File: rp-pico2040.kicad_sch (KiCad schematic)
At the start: 0 parts

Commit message: update components, pending route signals of connectors
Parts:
- added A1: RaspberryPi_Pico, Module:RaspberryPi_Pico_Common_Unspecified, symbol MCU_Module:RaspberryPi_Pico
- added D6: GREEN, LED_SMD:LED_1206_3216Metric, symbol Device:LED
- added D7, D8: RED, LED_SMD:LED_1206_3216Metric, symbol Device:LED
- added D9: SM4005PL-TP, symbol Device:D_Schottky
- added J3: Conn_01x07, symbol Connector_Generic:Conn_01x07
- added J4, J5: Conn_01x02, symbol Connector_Generic:Conn_01x02
- added J6: Conn_01x04, symbol Connector_Generic:Conn_01x04
- added R10, R11, R12: 1k, Resistor_SMD:R_1206_3216Metric, symbol Device:R
- added SW2, SW3: SW_Push, symbol Switch:SW_Push
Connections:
- new net: D8.2 (A), R12.1
- new net: A1.15 (GPIO11), SW2.2
- new net: A1.32 (GPIO27_ADC1), R12.2
- new net: D7.2 (A), R11.1
- new net: A1.1 (GPIO0), J3.1 (Pin_1)
- new net: A1.2 (GPIO1), J3.2 (Pin_2)
- new net: A1.4 (GPIO2), J3.3 (Pin_3)
- new net: A1.5 (GPIO3), J3.4 (Pin_4)
- new net: A1.6 (GPIO4), J3.5 (Pin_5)
- new net: A1.7 (GPIO5), J3.6 (Pin_6)
- new net: A1.34 (GPIO28_ADC2), SW3.1
- new net: A1.39 (VSYS), D9.1 (K)
- new net: D9.2 (A), J4.1 (Pin_1)
- new net: A1.10 (GPIO7), R11.2
- new net: A1.9 (GPIO6), R10.2
- new net: D6.2 (A), R10.1
- new net CHARGED: A1.24 (GPIO18), A1.31 (GPIO26_ADC0)
- new net GND: A1.13 (GND), A1.18 (GND), A1.23 (GND), A1.28 (GND), A1.3 (GND), A1.33 (AGND), A1.38 (GND), A1.8 (GND), D6.1 (K), D7.1 (K), D8.1 (K), J3.7 (Pin_7), J4.2 (Pin_2), SW2.1
- new net HVPULSE: A1.19 (GPIO14)
- new net HVPWM: A1.26 (GPIO20)
- new net VCC: A1.36 (3V3), SW3.2
- no-connect marks 0 -> 15

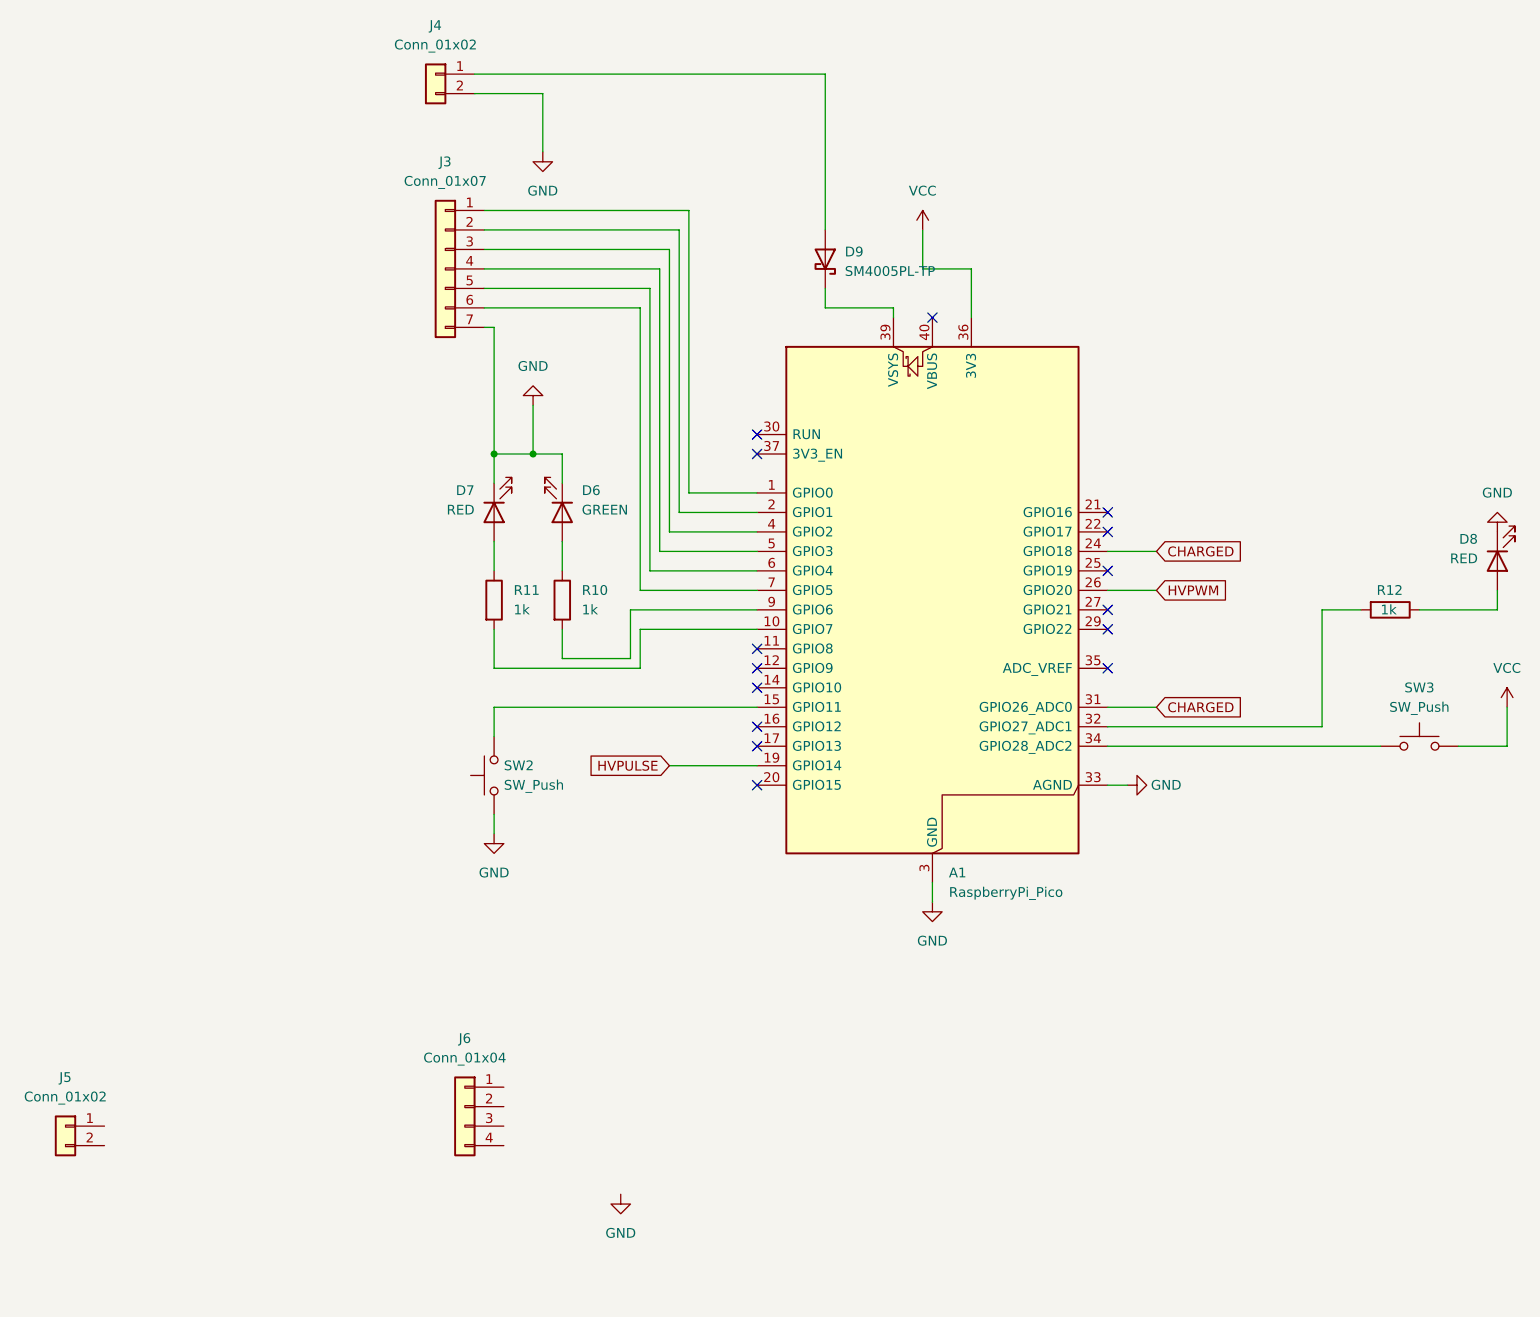
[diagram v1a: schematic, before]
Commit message: update components and footprints
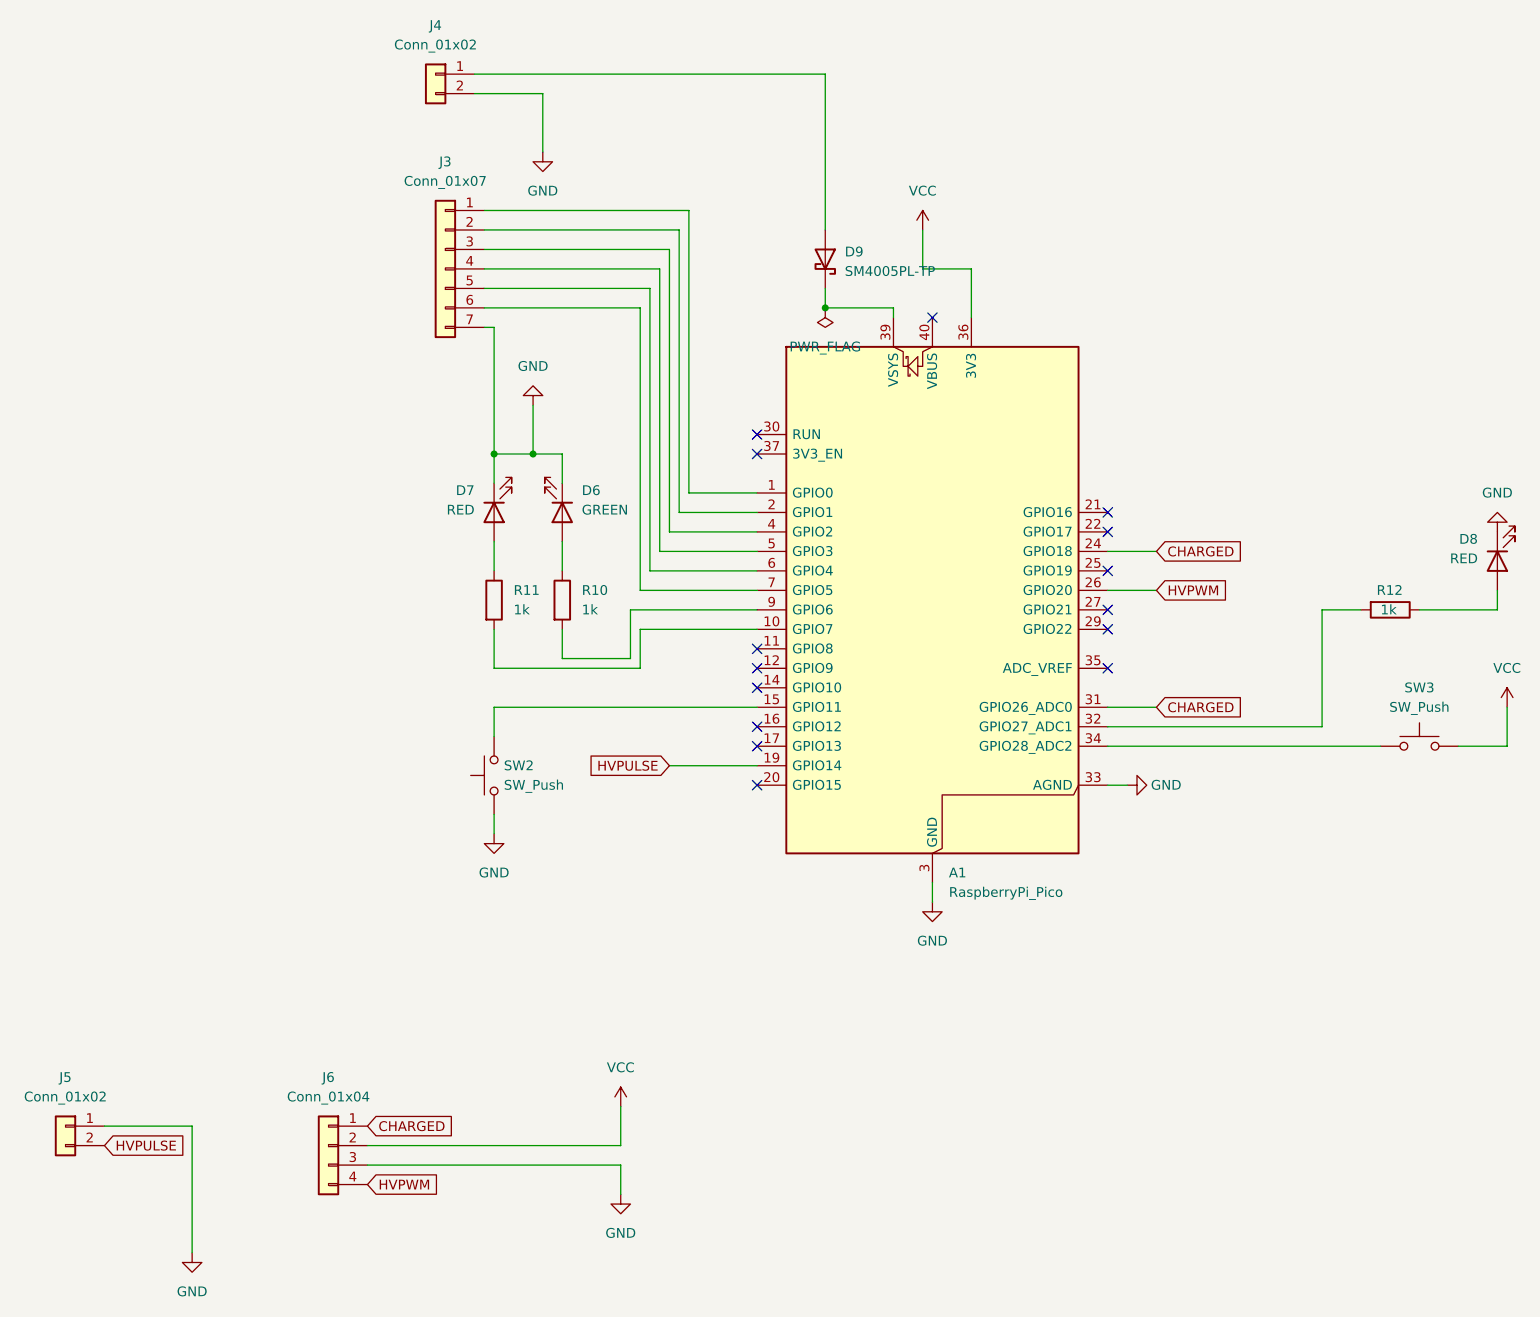
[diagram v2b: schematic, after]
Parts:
- D6: PART_NUMBER_LCSC (none) -> C3646937
- D7: PART_NUMBER_LCSC (none) -> C434444
- D8: PART_NUMBER_LCSC (none) -> C3646938
- D9: footprint (none) -> Diode_SMD:Nexperia_CFP3_SOD-123W; PART_NUMBER_LCSC (none) -> C330237
- J3: footprint (none) -> Connector_PinHeader_2.54mm:PinHeader_1x07_P2.54mm_Vertical
- J4, J5: footprint (none) -> Connector_PinHeader_2.54mm:PinHeader_1x02_P2.54mm_Vertical
- J6: footprint (none) -> Connector_PinHeader_2.54mm:PinHeader_1x04_P2.54mm_Vertical
- R10, R11, R12: PART_NUMBER_LCSC (none) -> C4410
- SW2, SW3: footprint (none) -> Button_Switch_SMD:SW_SPST_CK_RS282G05A3; PART_NUMBER_LCSC (none) -> C318938
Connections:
- net CHARGED: now also J6.1 (Pin_1)
- net GND: now also J5.1 (Pin_1), J6.3 (Pin_3)
- net HVPULSE: now also J5.2 (Pin_2)
- net HVPWM: now also J6.4 (Pin_4)
- net VCC: now also J6.2 (Pin_2)
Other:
- moved on the sheet: J6
